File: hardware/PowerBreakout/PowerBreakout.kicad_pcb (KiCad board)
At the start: 2 copper layers, 64.8 x 27.9 mm, 7 parts, among them J1 Screw_Terminal_01x02, J2 Conn_01x02_Male, U1 LM2596Adj

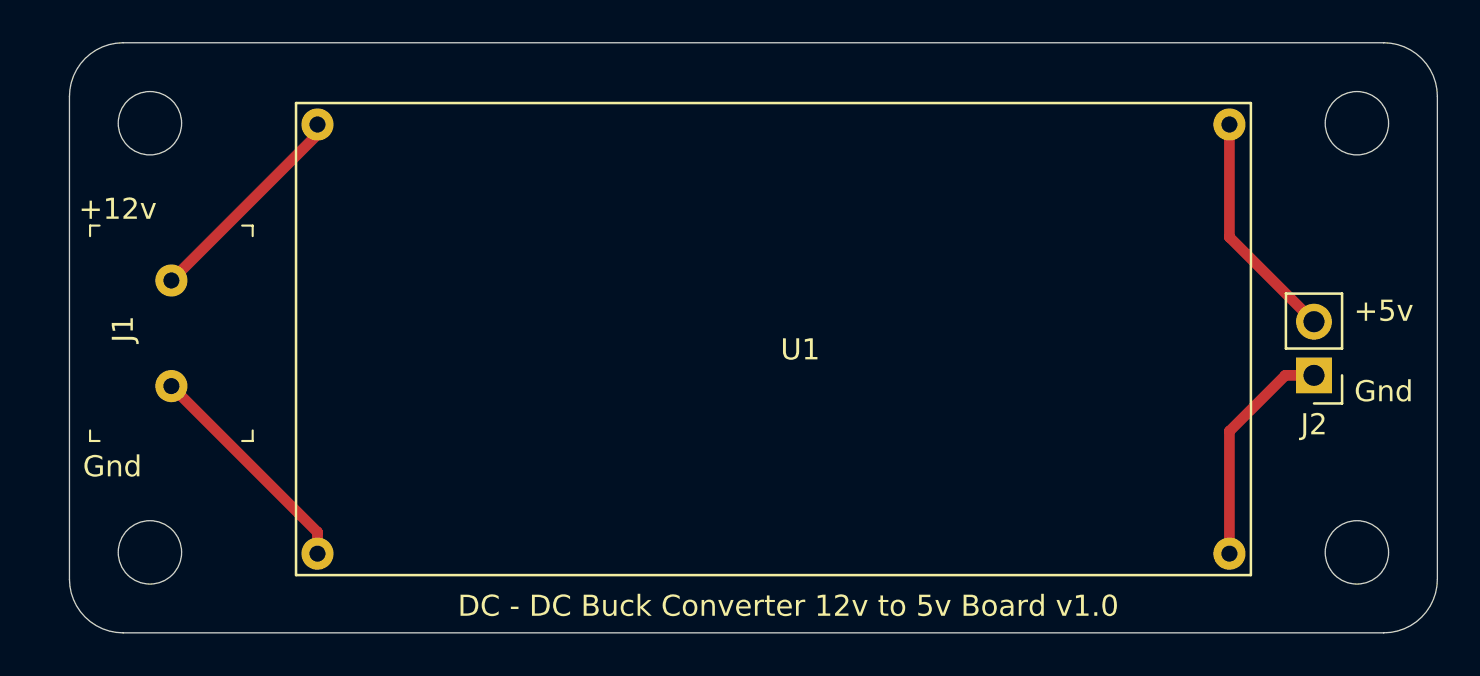
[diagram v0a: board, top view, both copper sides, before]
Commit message: fixing power breakout board and footprint with proper dimensions
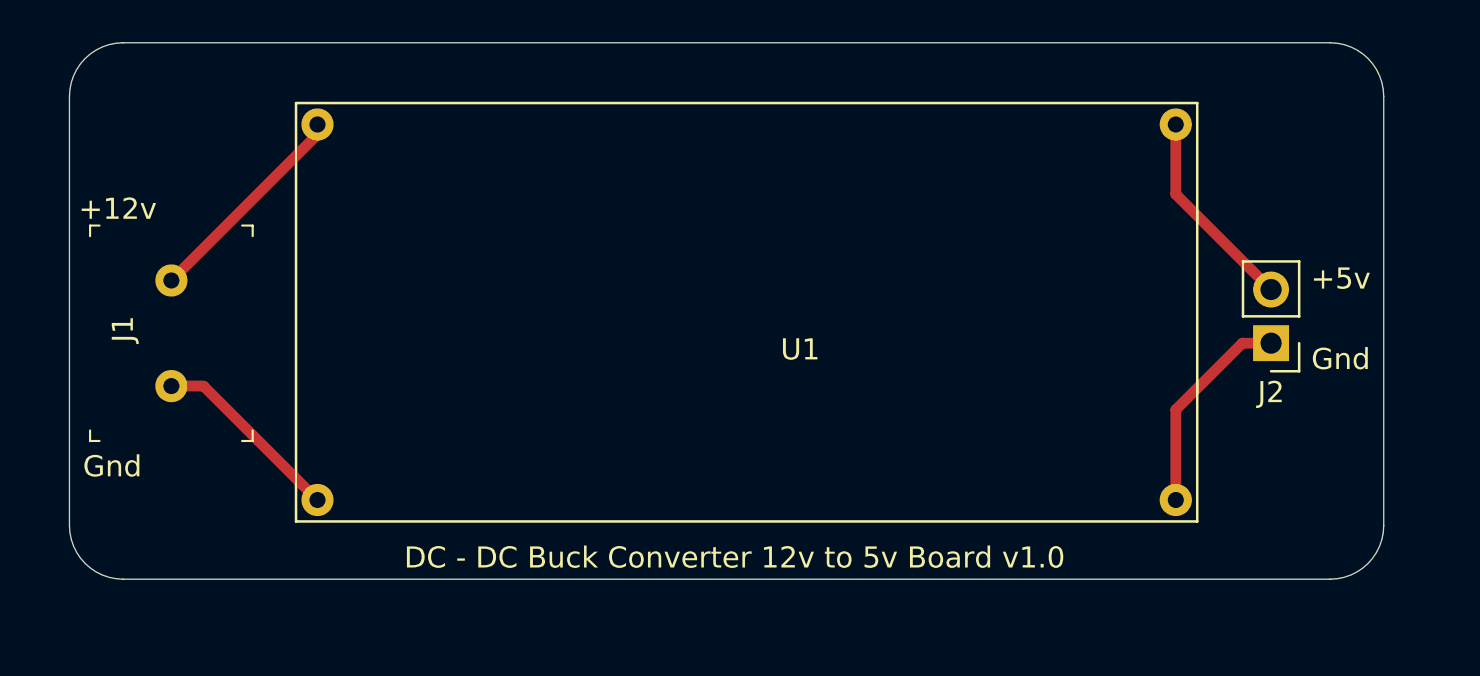
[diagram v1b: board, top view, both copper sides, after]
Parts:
- removed  : MountingHole_3mm, MountingHole:MountingHole_3mm (x4)
- moved J2 2.54 mm to (171.2, 72.6)
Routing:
- net Net-(J1-Pad1): track 10.8 -> 9.15 mm
- net Net-(J2-Pad2): track 11.0 -> 9.68 mm
- net Net-(J2-Pad1): track 10.9 -> 10.1 mm
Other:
- board size 64.8 x 27.9 mm -> 62.2 x 25.4 mm
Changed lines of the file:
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@@
     (tracks 9)
     (zones 0)
-    (modules 7)
+    (modules 3)
     (nets 5)
   )
@@
   )
   (setup
-    (last_trace_width 0.25)
+    (last_trace_width 0.508)
     (user_trace_width 0.508)
     (trace_clearance 0.2)
@@
     (add_net "Net-(J2-Pad2)")
   )
-  (module MountingHole:MountingHole_3mm (layer F.Cu)
-    (at 175.26 62.23)
-    (descr "Mounting Hole 3mm, no annular")
-    (tags "mounting hole 3mm no annular")
-    (attr virtual)
-    (fp_text reference " " (at 0 -4) (layer F.SilkS)
-      (effects (font (size 1 1) (thickness 0.15)))
-    )
-    (fp_text value MountingHole_3mm (at 0 4) (layer F.Fab)
-      (effects (font (size 1 1) (thickness 0.15)))
-    )
-    (fp_circle (center 0 0) (end 3.25 0) (layer F.CrtYd) (width 0.05))
-    (fp_circle (center 0 0) (end 3 0) (layer Cmts.User) (width 0.15))
-    (fp_text user %R (at 0.3 0) (layer F.Fab)
-      (effects (font (size 1 1) (thickness 0.15)))
-    )
-    (pad 1 np_thru_hole circle (at 0 0) (size 3 3) (drill 3) (layers *.Cu *.Mask))
-  )
-  (module MountingHole:MountingHole_3mm (layer F.Cu)
-    (at 175.26 82.55)
-    (descr "Mounting Hole 3mm, no annular")
-    (tags "mounting hole 3mm no annular")
-    (attr virtual)
-    (fp_text reference " " (at 0 -4) (layer F.SilkS)
-      (effects (font (size 1 1) (thickness 0.15)))
-    )
-    (fp_text value MountingHole_3mm (at 0 4) (layer F.Fab)
-      (effects (font (size 1 1) (thickness 0.15)))
-    )
-    (fp_circle (center 0 0) (end 3.25 0) (layer F.CrtYd) (width 0.05))
-    (fp_circle (center 0 0) (end 3 0) (layer Cmts.User) (width 0.15))
-    (fp_text user %R (at 0.3 0) (layer F.Fab)
-      (effects (font (size 1 1) (thickness 0.15)))
-    )
-    (pad 1 np_thru_hole circle (at 0 0) (size 3 3) (drill 3) (layers *.Cu *.Mask))
-  )
-  (module MountingHole:MountingHole_3mm (layer F.Cu)
-    (at 118.11 82.55)
-    (descr "Mounting Hole 3mm, no annular")
-    (tags "mounting hole 3mm no annular")
-    (attr virtual)
-    (fp_text reference " " (at 0 -4) (layer F.SilkS)
-      (effects (font (size 1 1) (thickness 0.15)))
-    )
-    (fp_text value MountingHole_3mm (at 0 4) (layer F.Fab)
-      (effects (font (size 1 1) (thickness 0.15)))
-    )
-    (fp_circle (center 0 0) (end 3.25 0) (layer F.CrtYd) (width 0.05))
-    (fp_circle (center 0 0) (end 3 0) (layer Cmts.User) (width 0.15))
-    (fp_text user %R (at 0.3 0) (layer F.Fab)
-      (effects (font (size 1 1) (thickness 0.15)))
-    )
-    (pad 1 np_thru_hole circle (at 0 0) (size 3 3) (drill 3) (layers *.Cu *.Mask))
-  )
-  (module MountingHole:MountingHole_3mm (layer F.Cu)
-    (at 118.11 62.23)
-    (descr "Mounting Hole 3mm, no annular")
-    (tags "mounting hole 3mm no annular")
-    (attr virtual)
-    (fp_text reference " " (at 0 -4) (layer F.SilkS)
-      (effects (font (size 1 1) (thickness 0.15)))
-    )
-    (fp_text value MountingHole_3mm (at 0 4) (layer F.Fab)
-      (effects (font (size 1 1) (thickness 0.15)))
-    )
-    (fp_circle (center 0 0) (end 3.25 0) (layer F.CrtYd) (width 0.05))
-    (fp_circle (center 0 0) (end 3 0) (layer Cmts.User) (width 0.15))
-    (fp_text user %R (at 0.3 0) (layer F.Fab)
-      (effects (font (size 1 1) (thickness 0.15)))
-    )
-    (pad 1 np_thru_hole circle (at 0 0) (size 3 3) (drill 3) (layers *.Cu *.Mask))
+  (module PowerBreakout:LM2596Adj (layer F.Cu)
+    (at 148.904001 72.450001)
+    (fp_text reference U1 (at 0 0.5) (layer F.SilkS)
+      (effects (font (size 1 1) (thickness 0.15)))
+    )
+    (fp_text value LM2596Adj (at 0 -1.524) (layer F.Fab)
+      (effects (font (size 1 1) (thickness 0.15)))
+    )
+    (fp_line (start 18.796 -11.176) (end -23.876 -11.176) (layer F.SilkS) (width 0.12))
+    (fp_line (start 18.796 8.636) (end 18.796 -11.176) (layer F.SilkS) (width 0.12))
+    (fp_line (start -23.876 8.636) (end 18.796 8.636) (layer F.SilkS) (width 0.12))
+    (fp_line (start -23.876 -11.176) (end -23.876 8.636) (layer F.SilkS) (width 0.12))
+    (pad 4 thru_hole circle (at 17.78 7.62) (size 1.524 1.524) (drill 0.762) (layers *.Cu *.Mask)
+      (net 3 "Net-(J2-Pad1)"))
+    (pad 3 thru_hole circle (at 17.78 -10.16) (size 1.524 1.524) (drill 0.762) (layers *.Cu *.Mask)
+      (net 4 "Net-(J2-Pad2)"))
+    (pad 2 thru_hole circle (at -22.86 7.62) (size 1.524 1.524) (drill 0.762) (layers *.Cu *.Mask)
+      (net 1 "Net-(J1-Pad1)"))
+    (pad 1 thru_hole circle (at -22.86 -10.16) (size 1.524 1.524) (drill 0.762) (layers *.Cu *.Mask)
+      (net 2 "Net-(J1-Pad2)"))
   )
   (module digikey-footprints:Term_Block_1x2_P5mm (layer F.Cu)
@@
   )
   (module Connector_PinHeader_2.54mm:PinHeader_1x02_P2.54mm_Vertical (layer F.Cu)
-    (at 173.228 74.168 180)
+    (at 171.196 72.644 180)
     (descr "Through hole straight pin header, 1x02, 2.54mm pitch, single row")
     (tags "Through hole pin header THT 1x02 2.54mm single row")
@@
     )
   )
-  (module PowerBreakout:LM2596Adj (layer F.Cu)
-    (at 148.904001 72.450001)
-    (fp_text reference U1 (at 0 0.5) (layer F.SilkS)
-      (effects (font (size 1 1) (thickness 0.15)))
-    )
-    (fp_text value LM2596Adj (at 0 -1.524) (layer F.Fab)
-      (effects (font (size 1 1) (thickness 0.15)))
-    )
-    (fp_line (start -23.876 -11.176) (end -23.876 11.176) (layer F.SilkS) (width 0.12))
-    (fp_line (start -23.876 11.176) (end 21.336 11.176) (layer F.SilkS) (width 0.12))
-    (fp_line (start 21.336 11.176) (end 21.336 -11.176) (layer F.SilkS) (width 0.12))
-    (fp_line (start 21.336 -11.176) (end -23.876 -11.176) (layer F.SilkS) (width 0.12))
-    (pad 1 thru_hole circle (at -22.86 -10.16) (size 1.524 1.524) (drill 0.762) (layers *.Cu *.Mask)
-      (net 2 "Net-(J1-Pad2)"))
-    (pad 2 thru_hole circle (at -22.86 10.16) (size 1.524 1.524) (drill 0.762) (layers *.Cu *.Mask)
-      (net 1 "Net-(J1-Pad1)"))
-    (pad 3 thru_hole circle (at 20.32 -10.16) (size 1.524 1.524) (drill 0.762) (layers *.Cu *.Mask)
-      (net 4 "Net-(J2-Pad2)"))
-    (pad 4 thru_hole circle (at 20.32 10.16) (size 1.524 1.524) (drill 0.762) (layers *.Cu *.Mask)
-      (net 3 "Net-(J2-Pad1)"))
-  )
-  (gr_text "DC - DC Buck Converter 12v to 5v Board v1.0" (at 148.336 85.09) (layer F.SilkS)
+  (gr_text "DC - DC Buck Converter 12v to 5v Board v1.0" (at 145.796 82.804) (layer F.SilkS)
     (effects (font (size 1 1) (thickness 0.15)))
   )
@@
     (effects (font (size 1 1) (thickness 0.15)))
   )
-  (gr_text Gnd (at 176.53 74.93) (layer F.SilkS)
-    (effects (font (size 1 1) (thickness 0.15)))
-  )
-  (gr_text +5v (at 176.53 71.12) (layer F.SilkS)
-    (effects (font (size 1 1) (thickness 0.15)))
-  )
-  (gr_arc (start 176.53 60.96) (end 179.07 60.96) (angle -90) (layer Edge.Cuts) (width 0.05))
-  (gr_arc (start 176.53 83.82) (end 176.53 86.36) (angle -90) (layer Edge.Cuts) (width 0.05))
-  (gr_arc (start 116.84 83.82) (end 114.3 83.82) (angle -90) (layer Edge.Cuts) (width 0.05))
+  (gr_text Gnd (at 174.498 73.406) (layer F.SilkS)
+    (effects (font (size 1 1) (thickness 0.15)))
+  )
+  (gr_text +5v (at 174.498 69.596) (layer F.SilkS)
+    (effects (font (size 1 1) (thickness 0.15)))
+  )
+  (gr_arc (start 173.99 60.96) (end 176.53 60.96) (angle -90) (layer Edge.Cuts) (width 0.05))
+  (gr_arc (start 173.99 81.28) (end 173.99 83.82) (angle -90) (layer Edge.Cuts) (width 0.05))
+  (gr_arc (start 116.84 81.28) (end 114.3 81.28) (angle -90) (layer Edge.Cuts) (width 0.05))
   (gr_arc (start 116.84 60.96) (end 116.84 58.42) (angle -90) (layer Edge.Cuts) (width 0.05))
-  (gr_line (start 114.3 83.82) (end 114.3 60.96) (layer Edge.Cuts) (width 0.05))
-  (gr_line (start 176.53 86.36) (end 116.84 86.36) (layer Edge.Cuts) (width 0.05))
-  (gr_line (start 179.07 60.96) (end 179.07 83.82) (layer Edge.Cuts) (width 0.05))
-  (gr_line (start 116.84 58.42) (end 176.53 58.42) (layer Edge.Cuts) (width 0.05))
-  (segment (start 126.044001 81.594001) (end 126.044001 82.610001) (width 0.508) (layer F.Cu) (net 1))
-  (segment (start 119.126 74.676) (end 126.044001 81.594001) (width 0.508) (layer F.Cu) (net 1))
+  (gr_line (start 114.3 81.28) (end 114.3 60.96) (layer Edge.Cuts) (width 0.05))
+  (gr_line (start 173.99 83.82) (end 116.84 83.82) (layer Edge.Cuts) (width 0.05))
+  (gr_line (start 176.53 60.96) (end 176.53 81.28) (layer Edge.Cuts) (width 0.05))
+  (gr_line (start 116.84 58.42) (end 173.99 58.42) (layer Edge.Cuts) (width 0.05))
+  (segment (start 120.65 74.676) (end 126.044001 80.070001) (width 0.508) (layer F.Cu) (net 1))
+  (segment (start 119.126 74.676) (end 120.65 74.676) (width 0.508) (layer F.Cu) (net 1))
   (segment (start 126.044001 62.757999) (end 126.044001 62.290001) (width 0.508) (layer F.Cu) (net 2))
   (segment (start 119.126 69.676) (end 126.044001 62.757999) (width 0.508) (layer F.Cu) (net 2))
-  (segment (start 171.87 74.168) (end 173.228 74.168) (width 0.508) (layer F.Cu) (net 3))
-  (segment (start 169.224001 76.813999) (end 171.87 74.168) (width 0.508) (layer F.Cu) (net 3))
-  (segment (start 169.224001 82.610001) (end 169.224001 76.813999) (width 0.508) (layer F.Cu) (net 3))
-  (segment (start 169.224001 67.624001) (end 173.228 71.628) (width 0.508) (layer F.Cu) (net 4))
-  (segment (start 169.224001 62.290001) (end 169.224001 67.624001) (width 0.508) (layer F.Cu) (net 4))
+  (segment (start 169.838 72.644) (end 171.196 72.644) (width 0.508) (layer F.Cu) (net 3))
+  (segment (start 166.684001 75.797999) (end 169.838 72.644) (width 0.508) (layer F.Cu) (net 3))
+  (segment (start 166.684001 80.070001) (end 166.684001 75.797999) (width 0.508) (layer F.Cu) (net 3))
+  (segment (start 166.684001 65.592001) (end 166.684001 62.290001) (width 0.508) (layer F.Cu) (net 4))
+  (segment (start 171.196 70.104) (end 166.684001 65.592001) (width 0.508) (layer F.Cu) (net 4))
 )

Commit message: fixing hole size for screw terminals (manually modified footprint) and generating gerbers
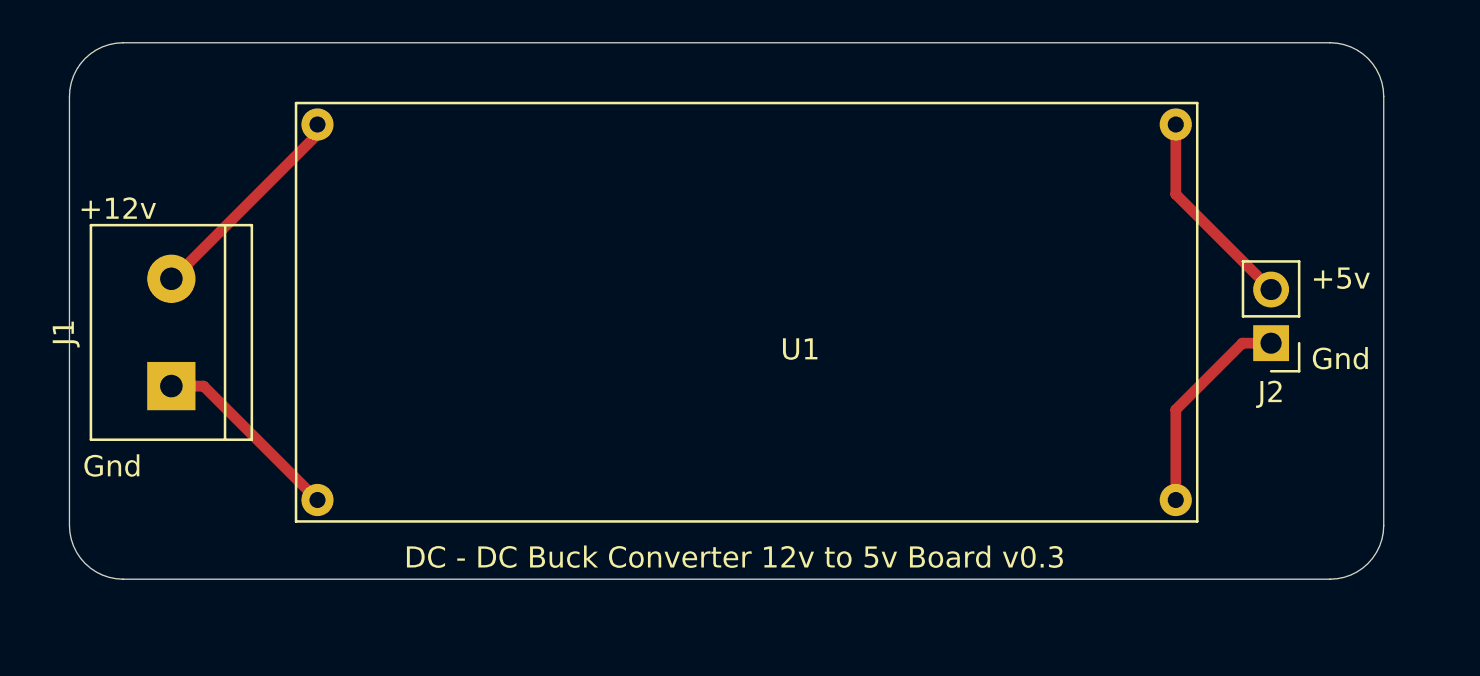
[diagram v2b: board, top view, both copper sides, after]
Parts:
- J1: footprint digikey-footprints:Term_Block_1x2_P5mm -> TerminalBlock:TerminalBlock_bornier-2_P5.08mm
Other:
- board text added: "DC - DC Buck Converter 12v to 5v Board v0.3"
- board text removed: "DC - DC Buck Converter 12v to 5v Board v1.0"
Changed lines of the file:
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@@
   )
   (setup
-    (last_trace_width 0.508)
+    (last_trace_width 0.25)
     (user_trace_width 0.508)
     (trace_clearance 0.2)
@@
     (mod_text_size 1 1)
     (mod_text_width 0.15)
-    (pad_size 1.524 1.524)
-    (pad_drill 0.762)
+    (pad_size 2.286 2.286)
+    (pad_drill 1.0668)
     (pad_to_mask_clearance 0.051)
     (solder_mask_min_width 0.25)
@@
       (net 2 "Net-(J1-Pad2)"))
   )
-  (module digikey-footprints:Term_Block_1x2_P5mm (layer F.Cu)
-    (at 119.126 74.676 90)
-    (descr http://www.on-shore.com/wp-content/uploads/2015/09/osttcxx0162.pdf)
-    (fp_text reference J1 (at 2.7 -2.286 90) (layer F.SilkS)
-      (effects (font (size 1 1) (thickness 0.15)))
-    )
-    (fp_text value Screw_Terminal_01x02 (at 2.05 5.05 90) (layer F.Fab)
-      (effects (font (size 1 1) (thickness 0.15)))
-    )
-    (fp_text user %R (at 2.5 0 90) (layer F.Fab)
-      (effects (font (size 1 1) (thickness 0.15)))
-    )
-    (fp_line (start 7.6 3.85) (end 7.1 3.85) (layer F.SilkS) (width 0.1))
-    (fp_line (start 7.6 3.85) (end 7.6 3.35) (layer F.SilkS) (width 0.1))
-    (fp_line (start -2.6 3.85) (end -2.6 3.35) (layer F.SilkS) (width 0.1))
-    (fp_line (start -2.6 3.85) (end -2.1 3.85) (layer F.SilkS) (width 0.1))
-    (fp_line (start -2.6 -3.85) (end -2.1 -3.85) (layer F.SilkS) (width 0.1))
-    (fp_line (start -2.6 -3.85) (end -2.6 -3.4) (layer F.SilkS) (width 0.1))
-    (fp_line (start 7.6 -3.85) (end 7.6 -3.4) (layer F.SilkS) (width 0.1))
-    (fp_line (start 7.6 -3.85) (end 7.1 -3.85) (layer F.SilkS) (width 0.1))
-    (fp_line (start -2.75 -4) (end 7.75 -4) (layer F.CrtYd) (width 0.05))
-    (fp_line (start 7.75 -4) (end 7.75 4) (layer F.CrtYd) (width 0.05))
-    (fp_line (start -2.75 4) (end 7.75 4) (layer F.CrtYd) (width 0.05))
-    (fp_line (start 7.5 -3.75) (end 7.5 3.75) (layer F.Fab) (width 0.1))
-    (fp_line (start 7.5 3.75) (end -2.5 3.75) (layer F.Fab) (width 0.1))
-    (fp_line (start 7.5 -3.75) (end -2.5 -3.75) (layer F.Fab) (width 0.1))
-    (fp_line (start -2.75 -4) (end -2.75 4) (layer F.CrtYd) (width 0.05))
-    (fp_line (start -2.5 -3.75) (end -2.5 3.75) (layer F.Fab) (width 0.1))
-    (pad 1 thru_hole circle (at 0 0 90) (size 1.524 1.524) (drill 0.762) (layers *.Cu *.Mask)
-      (net 1 "Net-(J1-Pad1)"))
-    (pad 2 thru_hole circle (at 5 0 90) (size 1.524 1.524) (drill 0.762) (layers *.Cu *.Mask)
-      (net 2 "Net-(J1-Pad2)"))
-  )
   (module Connector_PinHeader_2.54mm:PinHeader_1x02_P2.54mm_Vertical (layer F.Cu)
     (at 171.196 72.644 180)
@@
     )
   )
-  (gr_text "DC - DC Buck Converter 12v to 5v Board v1.0" (at 145.796 82.804) (layer F.SilkS)
+  (module TerminalBlock:TerminalBlock_bornier-2_P5.08mm (layer F.Cu)
+    (at 119.126 74.676 90)
+    (descr "simple 2-pin terminal block, pitch 5.08mm, revamped version of bornier2")
+    (tags "terminal block bornier2")
+    (fp_text reference J1 (at 2.54 -5.08 90) (layer F.SilkS)
+      (effects (font (size 1 1) (thickness 0.15)))
+    )
+    (fp_text value Screw_Terminal_01x02 (at 2.54 5.08 90) (layer F.Fab)
+      (effects (font (size 1 1) (thickness 0.15)))
+    )
+    (fp_text user %R (at 2.54 0 90) (layer F.Fab)
+      (effects (font (size 1 1) (thickness 0.15)))
+    )
+    (fp_line (start -2.41 2.55) (end 7.49 2.55) (layer F.Fab) (width 0.1))
+    (fp_line (start -2.46 -3.75) (end -2.46 3.75) (layer F.Fab) (width 0.1))
+    (fp_line (start -2.46 3.75) (end 7.54 3.75) (layer F.Fab) (width 0.1))
+    (fp_line (start 7.54 3.75) (end 7.54 -3.75) (layer F.Fab) (width 0.1))
+    (fp_line (start 7.54 -3.75) (end -2.46 -3.75) (layer F.Fab) (width 0.1))
+    (fp_line (start 7.62 2.54) (end -2.54 2.54) (layer F.SilkS) (width 0.12))
+    (fp_line (start 7.62 3.81) (end 7.62 -3.81) (layer F.SilkS) (width 0.12))
+    (fp_line (start 7.62 -3.81) (end -2.54 -3.81) (layer F.SilkS) (width 0.12))
+    (fp_line (start -2.54 -3.81) (end -2.54 3.81) (layer F.SilkS) (width 0.12))
+    (fp_line (start -2.54 3.81) (end 7.62 3.81) (layer F.SilkS) (width 0.12))
+    (fp_line (start -2.71 -4) (end 7.79 -4) (layer F.CrtYd) (width 0.05))
+    (fp_line (start -2.71 -4) (end -2.71 4) (layer F.CrtYd) (width 0.05))
+    (fp_line (start 7.79 4) (end 7.79 -4) (layer F.CrtYd) (width 0.05))
+    (fp_line (start 7.79 4) (end -2.71 4) (layer F.CrtYd) (width 0.05))
+    (pad 1 thru_hole rect (at 0 0 90) (size 2.286 2.286) (drill 1.0668) (layers *.Cu *.Mask)
+      (net 1 "Net-(J1-Pad1)"))
+    (pad 2 thru_hole circle (at 5.08 0 90) (size 2.286 2.286) (drill 1.0668) (layers *.Cu *.Mask)
+      (net 2 "Net-(J1-Pad2)"))
+    (model ${KISYS3DMOD}/TerminalBlock.3dshapes/TerminalBlock_bornier-2_P5.08mm.wrl
+      (offset (xyz 2.539999961853027 0 0))
+      (scale (xyz 1 1 1))
+      (rotate (xyz 0 0 0))
+    )
+  )
+  (gr_text "DC - DC Buck Converter 12v to 5v Board v0.3" (at 145.796 82.804) (layer F.SilkS)
     (effects (font (size 1 1) (thickness 0.15)))
   )
